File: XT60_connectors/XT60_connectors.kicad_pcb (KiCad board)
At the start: 2 copper layers, 162.6 x 40.6 mm, 51 parts, among them J1 XT60-F, J10 XT60-F, J11 XT60-F, J2 XT60-F, J3 XT60_M, J4 XT60-F, J5 XT60-F, J6 XT60-F, J7 XT60-F, J8 XT60-F, J9 XT60-F

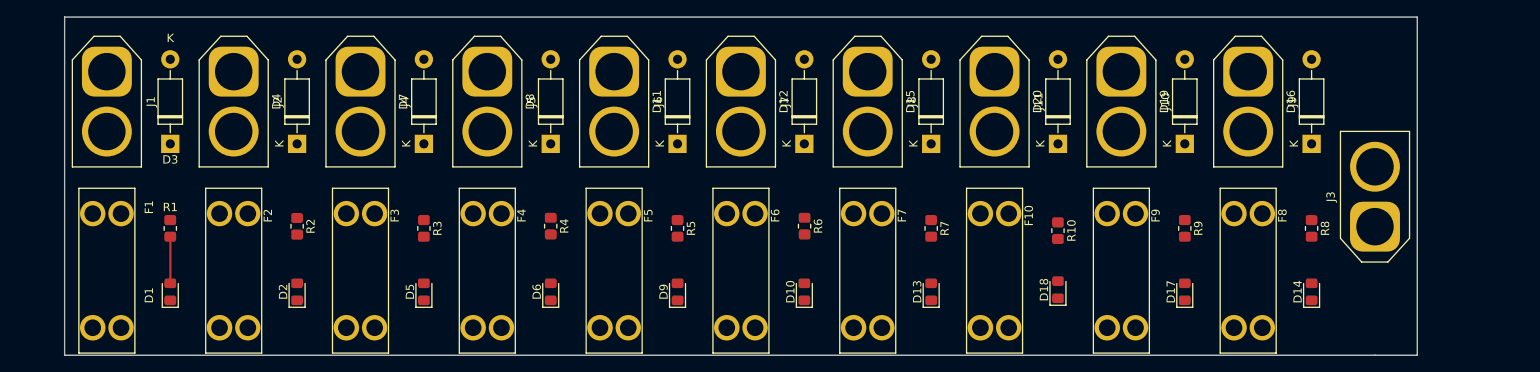
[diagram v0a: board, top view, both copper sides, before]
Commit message: power connector added
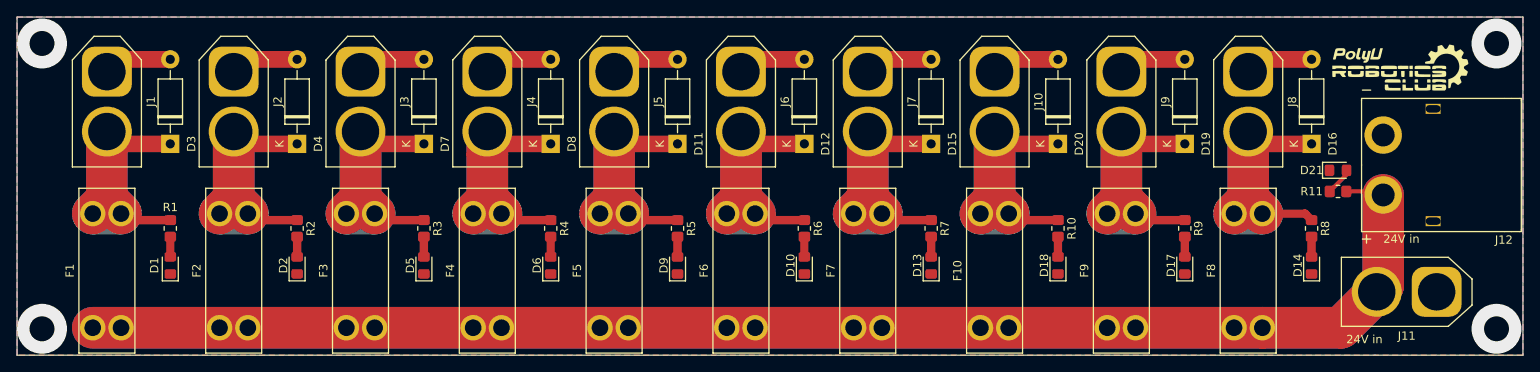
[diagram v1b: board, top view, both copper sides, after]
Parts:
- removed the J3 at (190.5, 65.8)
- added D21: power, LED_SMD:LED_0805_2012Metric_Pad1.15x1.40mm_HandSolder, F.Cu at (186.1, 59.1)
- added G***: LOGO, PolyuRobotics:Club_logo, F.Cu at (193.7, 47.0)
- added G***: LOGO, PolyuRobotics:Club_logo, B.Cu at (134.6, 71.1)
- added J11: XT60_M, Connector_AMASS:AMASS_XT60-M_1x02_P7.20mm_Vertical, F.Cu at (197.9, 73.7)
- added J12: XT90-M, PolyuRobotics:XT60PW-M20, F.Cu at (197.5, 58.4)
- added R11: 4K, Resistor_SMD:R_0805_2012Metric_Pad1.20x1.40mm_HandSolder, F.Cu at (186.1, 61.6)
- moved D1 3.17 mm to (45.7, 70.5)
- moved D10 3.17 mm to (121.9, 70.5)
- moved D13 3.17 mm to (137.2, 70.5)
- moved D14 3.17 mm to (182.9, 70.5)
- moved D17 3.17 mm to (167.6, 70.5)
- moved D2 3.17 mm to (61.0, 70.5)
- moved D5 3.17 mm to (76.2, 70.5)
- moved D6 3.17 mm to (91.4, 70.5)
- moved D9 3.17 mm to (106.7, 70.5)
- moved D18 2.93 mm to (152.4, 70.5)
- moved R6 0.27 mm to (121.9, 66.0)
- moved R4 0.27 mm to (91.4, 66.0)
- moved R10 0.27 mm to (152.4, 66.0)
- moved R2 0.25 mm to (61.0, 66.0)
- renumbered J11 to J10, J4 to J3, J5 to J4, J6 to J5, J7 to J6, J8 to J7, J9 to J8, J10 to J9
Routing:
- net +24V: track 0.00 -> 340.7 mm
- net GND: track 0.00 -> 82.3 mm
- net Net-(D11-Pad1): track 0.00 -> 43.8 mm
- net Net-(D7-Pad1): track 0.00 -> 43.8 mm
- net Net-(D12-Pad1): track 0.00 -> 43.8 mm
- net Net-(D4-Pad1): track 0.00 -> 43.8 mm
- net Net-(D3-Pad1): track 0.00 -> 43.8 mm
- net Net-(D16-Pad1): track 0.00 -> 43.8 mm
- net Net-(D15-Pad1): track 0.00 -> 43.8 mm
- net Net-(D8-Pad1): track 0.00 -> 43.8 mm
- net Net-(D19-Pad1): track 0.00 -> 43.8 mm
- net Net-(D20-Pad1): track 0.00 -> 43.8 mm
- net Net-(D21-Pad2): track 0.00 -> 3.38 mm
- net Net-(D1-Pad2): track 5.59 -> 2.42 mm
- net Net-(D9-Pad2): track 0.00 -> 2.42 mm
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- added copper zone on B.Cu, net GND
- added copper zone on F.Cu, net GND
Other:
- board size 162.6 x 40.6 mm -> 181 x 40.6 mm
- board text added: "24V in"
- board text added: "XT60 Power-Board Extender By SamsonChau 2022-04-20"
